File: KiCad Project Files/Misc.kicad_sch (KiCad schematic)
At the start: 2 parts, among them J2 SWD

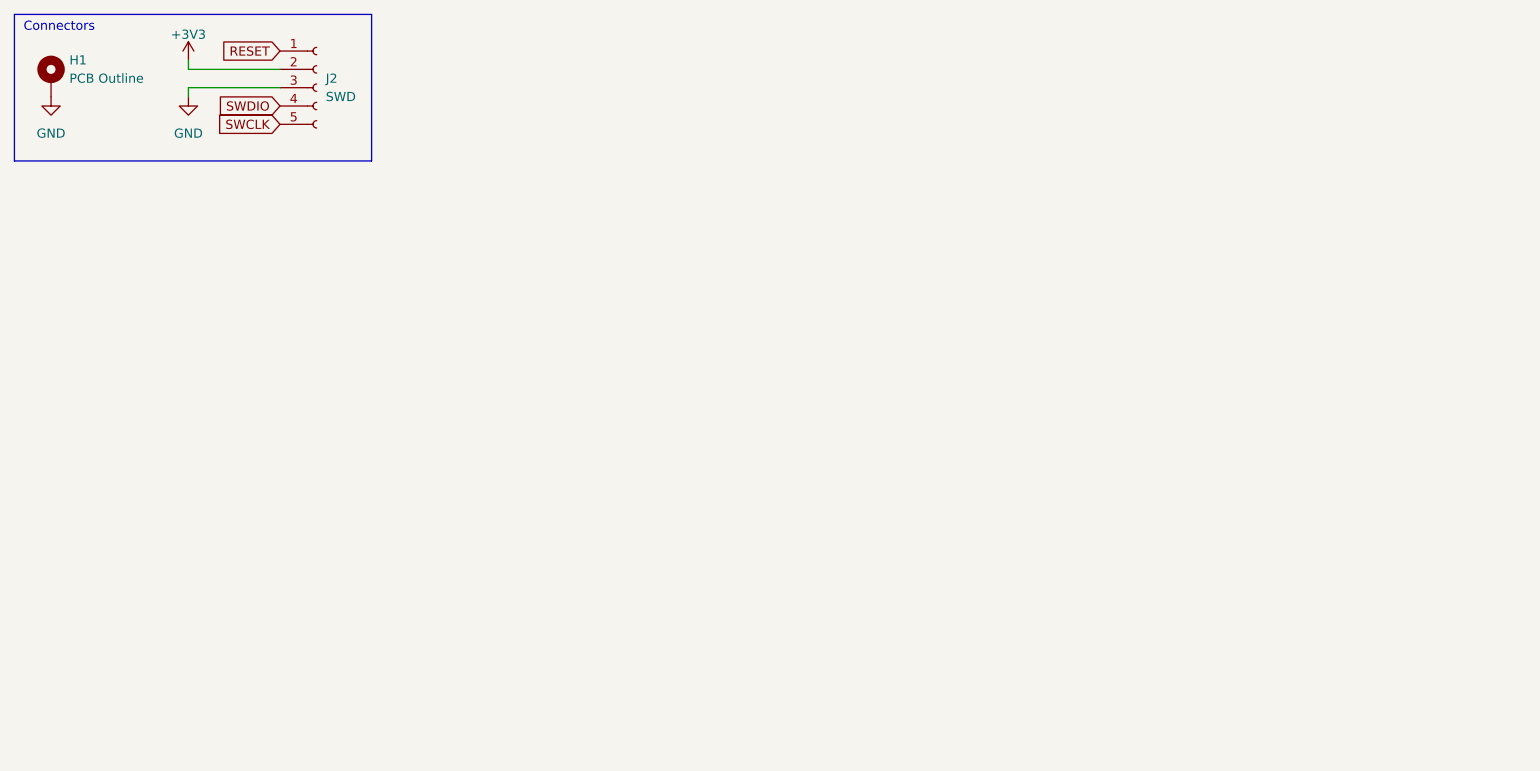
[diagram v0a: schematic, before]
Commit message: Add leds to pcb
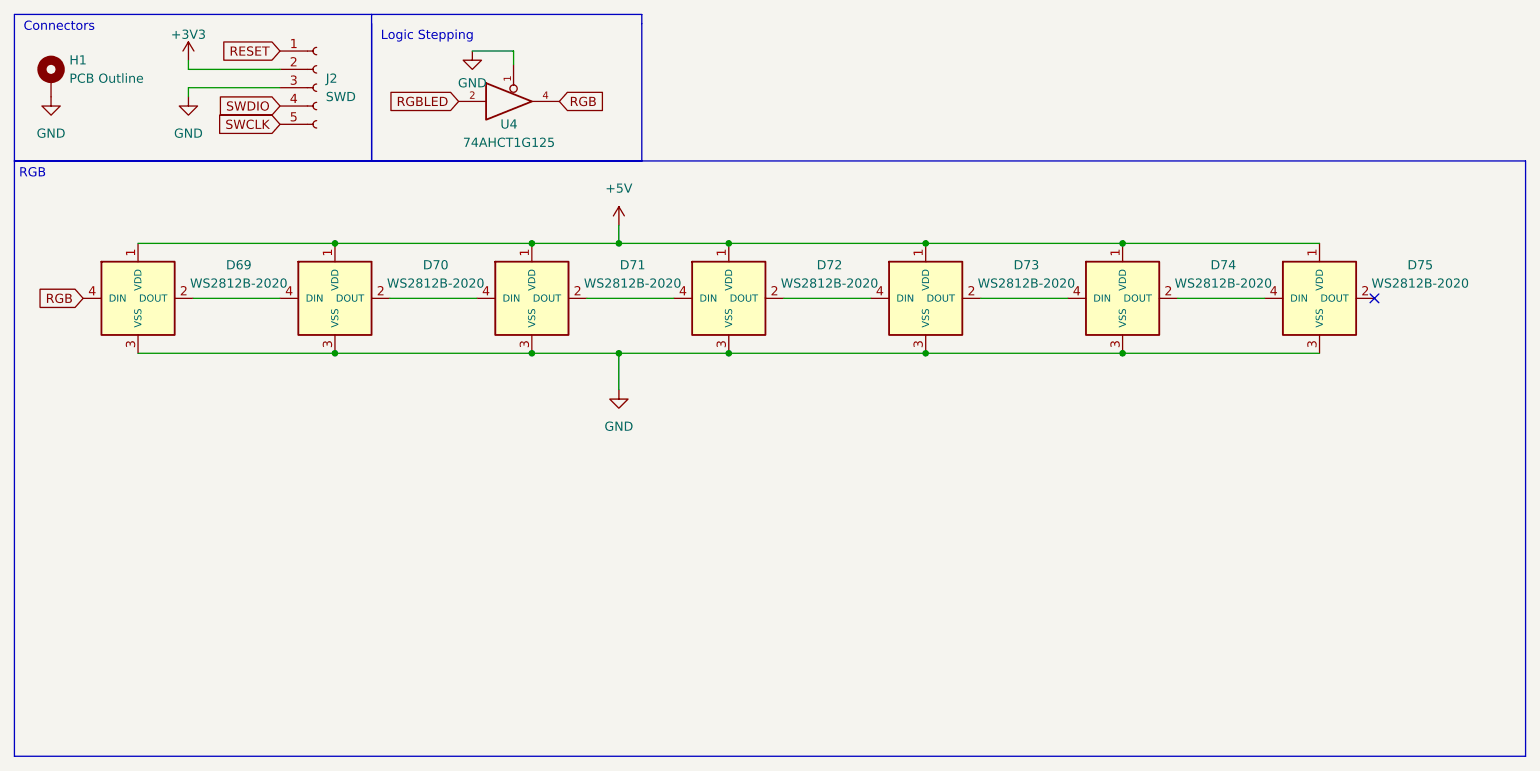
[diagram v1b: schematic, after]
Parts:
- added D69, D70, D71, D72, D73, D74, D75: WS2812B-2020, kbd:YS-SK6812MINI-E, symbol kbd:YS-SK6812MINI-E
- added U4: 74AHCT1G125, Package_TO_SOT_SMD:SOT-23-5, symbol 74xGxx:74AHCT1G125
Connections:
- net GND: now also D69.3 (VSS), D70.3 (VSS), D71.3 (VSS), D72.3 (VSS), D73.3 (VSS), D74.3 (VSS), D75.3 (VSS), U4.1, U4.3 (GND)
- new net: D71.2 (DOUT), D72.4 (DIN)
- new net: D70.2 (DOUT), D71.4 (DIN)
- new net: D74.2 (DOUT), D75.4 (DIN)
- new net: D73.2 (DOUT), D74.4 (DIN)
- new net: D69.2 (DOUT), D70.4 (DIN)
- new net: D72.2 (DOUT), D73.4 (DIN)
- new net +5V: D69.1 (VDD), D70.1 (VDD), D71.1 (VDD), D72.1 (VDD), D73.1 (VDD), D74.1 (VDD), D75.1 (VDD), U4.5 (+5V)
- new net RGB: D69.4 (DIN), U4.4
- new net RGBLED: U4.2
- no-connect marks 0 -> 1
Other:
- note added: "Logic Stepping"
- note added: "RGB"
